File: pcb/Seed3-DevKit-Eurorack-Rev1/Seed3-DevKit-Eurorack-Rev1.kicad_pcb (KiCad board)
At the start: 2 copper layers, 141.9 x 111 mm, 136 parts, among them J7 USB4110GFA, Q1 MMBT3904, Q2 MMBT3904, SW1 TOGGLE_ON_OFF_ON_PIP2, SW2 TOGGLE_ON-ON_PIP3, SW3 PTH Mini Button, SW4 PTH Mini Button, U1 TL072, U11 H11L1, U12 CD4051B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

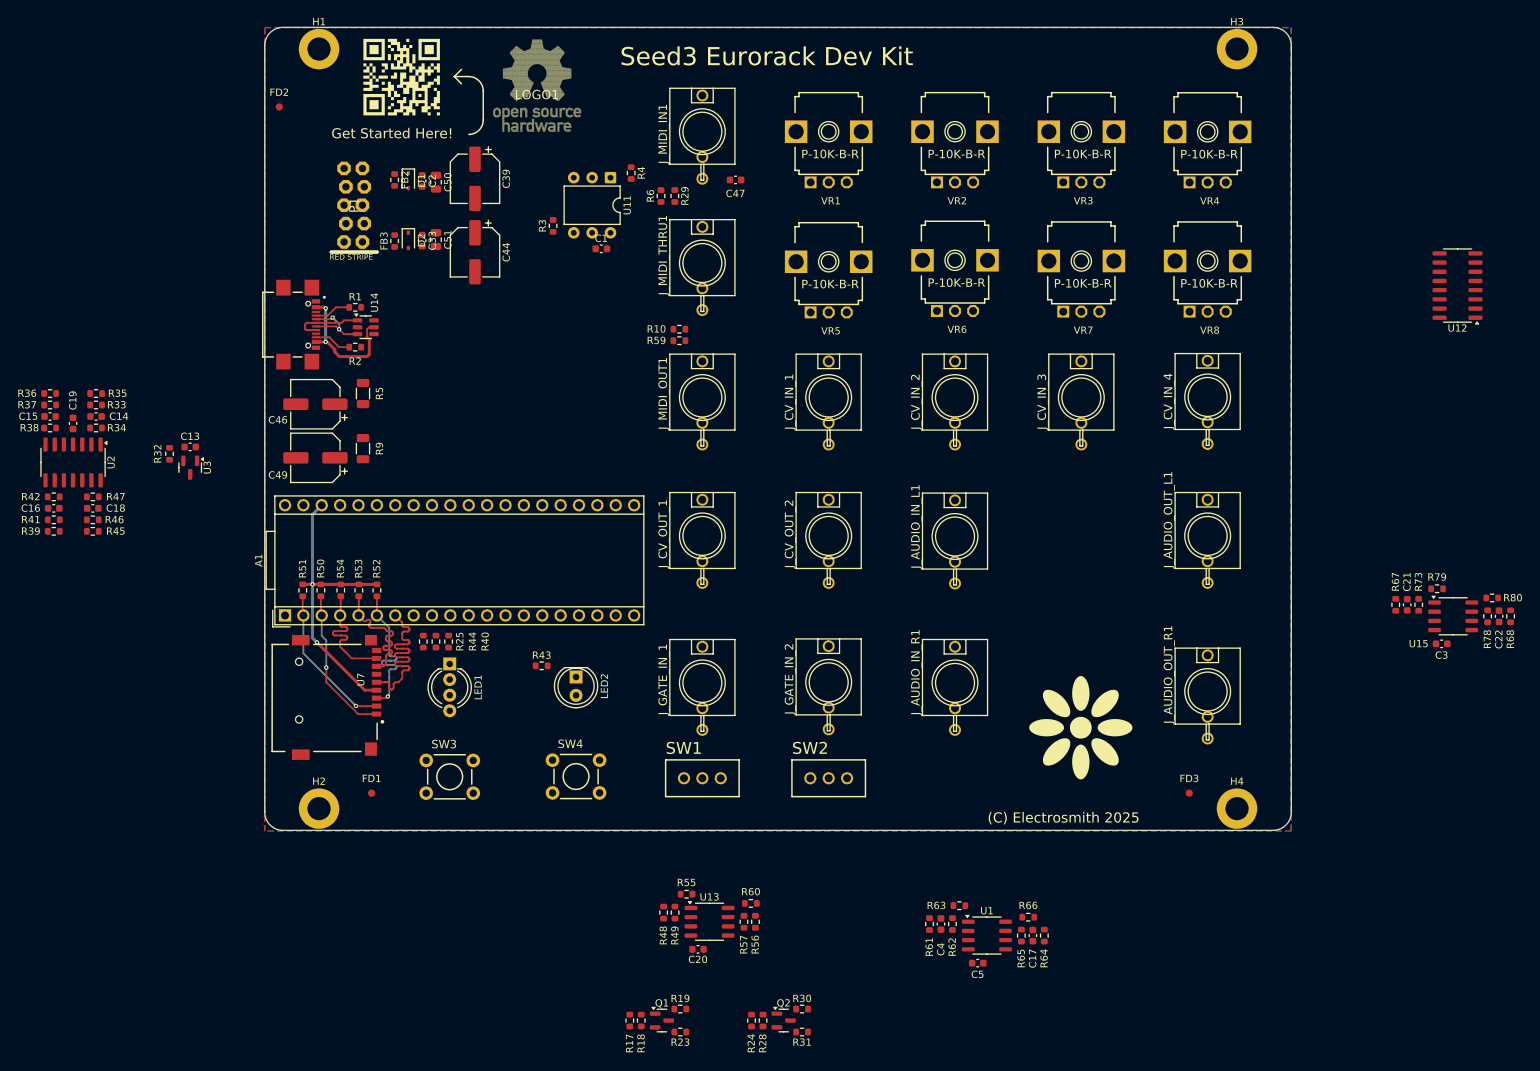
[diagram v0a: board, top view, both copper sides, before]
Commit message: finished routing board, fixed DRCs, and added cutout to PCB.
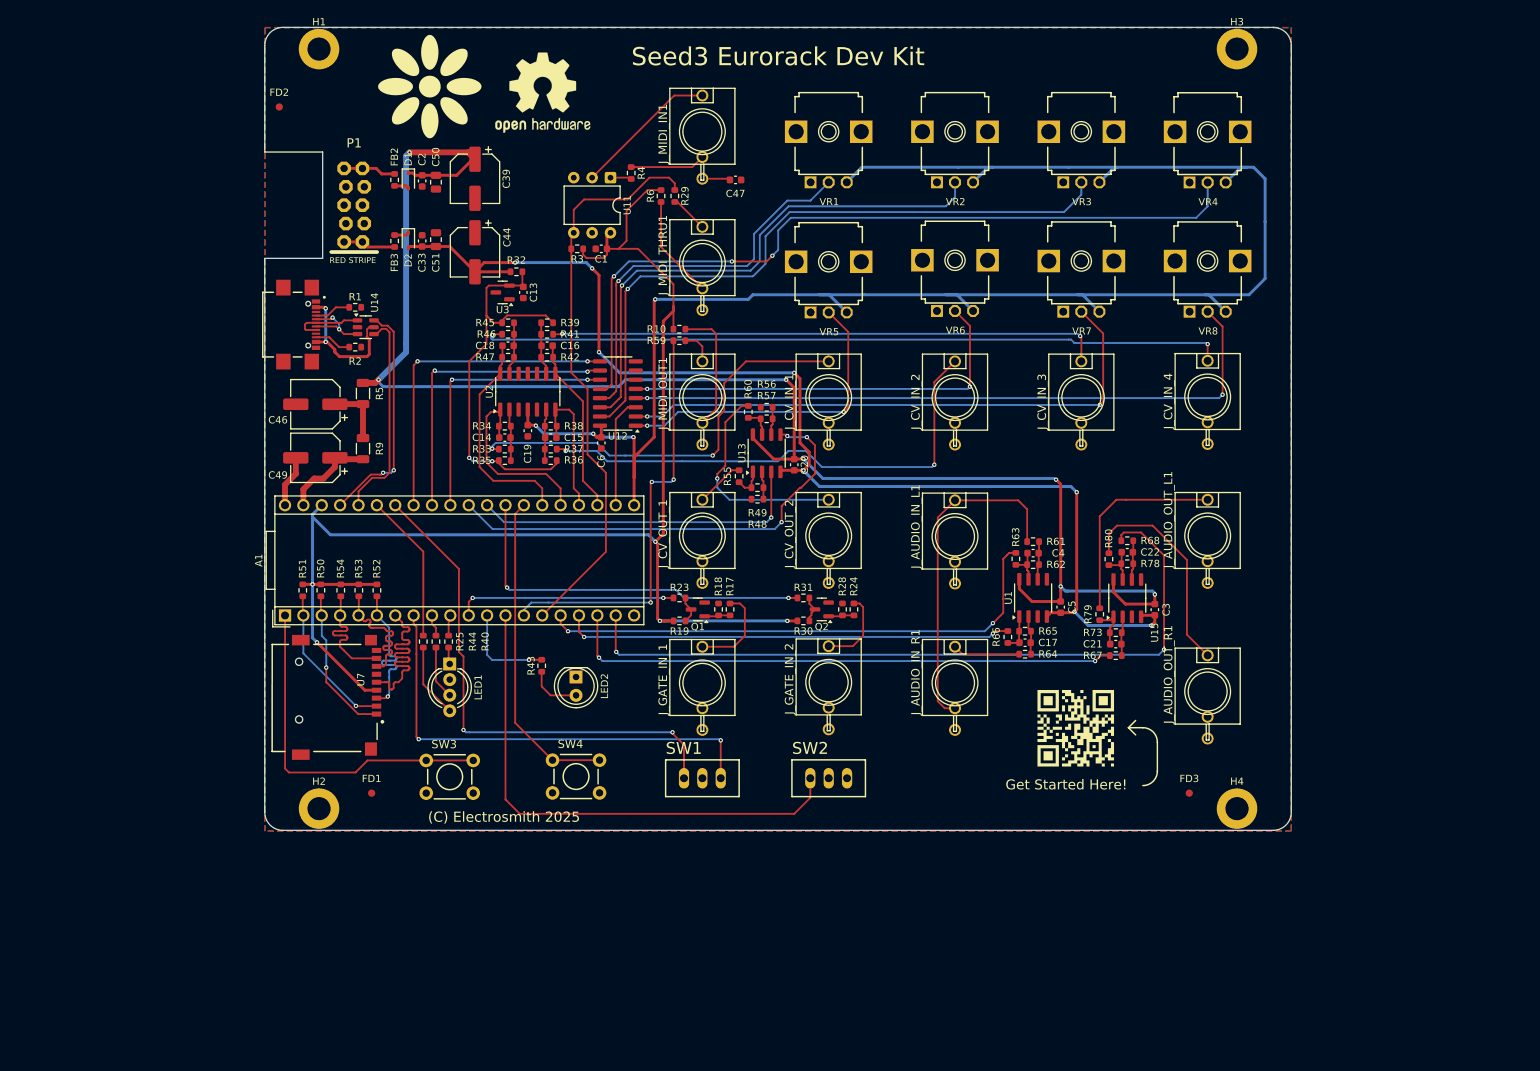
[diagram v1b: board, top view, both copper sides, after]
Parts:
- added C6: 100NF, Capacitor_SMD:C_0603_1608Metric, F.Cu at (96.5, 101.4)
- LOGO1: footprint parts-for-kicad:OSHW-LOGO-L_TEXT -> Symbol:OSHW-Logo2_14.6x12mm_SilkScreen
- SW1: footprint parts-for-kicad:TOGGLE_SILK_PIP3 -> parts-for-kicad:TOGGLE_ON_OFF_ON_SILK
- SW2: footprint parts-for-kicad:TOGGLE_SILK_PIP3 -> parts-for-kicad:TOGGLE_ON-ON_SILK
- VR1, VR2, VR3, VR4, VR5, VR6, VR7, VR8: footprint parts-for-kicad:9MM_SNAP-IN_POT_SILK_PIP -> parts-for-kicad:9MM_SNAP-IN_POT_SILK
- moved U12 117.0 mm to (98.8, 94.6)
- moved R39 74.0 mm to (89.0, 84.8), turned to 0 degrees
- moved R41 72.9 mm to (89.0, 86.4), turned to 0 degrees
- moved C16 71.8 mm to (89.0, 88.0), turned to 180 degrees
- moved R56 71.1 mm to (119.4, 96.5), turned to 180 degrees
- moved R42 70.9 mm to (89.0, 89.6), turned to 180 degrees
- moved R36 69.8 mm to (89.5, 103.9)
- moved R57 69.6 mm to (119.4, 98.1), turned to 0 degrees
- moved R37 69.5 mm to (89.5, 102.3), turned to 0 degrees
- moved C15 69.3 mm to (89.5, 100.7), turned to 180 degrees
- moved R38 69.2 mm to (89.5, 99.1), turned to 180 degrees
- moved C20 68.3 mm to (123.2, 104.5), turned to -90 degrees
- moved R60 67.9 mm to (116.8, 97.2), turned to -90 degrees
- moved U13 65.3 mm to (119.4, 102.9), turned to 90 degrees
- moved R45 64.2 mm to (83.6, 84.8), turned to 180 degrees
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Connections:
- A1 pad 10: TOG_1 -> LED_R
- A1 pad 13: /Daisy/MUX_CTRL_C -> TOG_1
- A1 pad 23: /Daisy/CV_1_ADC -> /Daisy/CV_3_ADC
- A1 pad 25: /Daisy/CV_3_ADC -> /Daisy/CV_1_ADC
- A1 pad 33: LED_R -> /Daisy/MUX_CTRL_C
- A1 pad 34: LED_B -> TOG_2_A
- A1 pad 9: TOG_2_A -> LED_B
- C17 pad 2: Net-(U1B--) -> Net-(U1A--)
- C4 pad 2: Net-(U1A--) -> Net-(U1B--)
- H1 pad 1: (no net) -> unconnected-(H1-Pad1)
- H2 pad 1: (no net) -> unconnected-(H2-Pad1)
- H3 pad 1: (no net) -> unconnected-(H3-Pad1)
- H4 pad 1: (no net) -> unconnected-(H4-Pad1)
- R61 pad 1: Net-(U1A--) -> Net-(U1B--)
- R62 pad 2: Net-(U1A--) -> Net-(U1B--)
- R64 pad 1: Net-(U1B--) -> Net-(U1A--)
- R65 pad 2: Net-(U1B--) -> Net-(U1A--)
- U1 pad 1: Net-(C4-Pad1) -> Net-(C17-Pad1)
- U1 pad 7: Net-(C17-Pad1) -> Net-(C4-Pad1)
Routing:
- net +3V3_A: track 0.00 -> 242.2 mm, vias 0 -> 4
- net +12V: track 0.00 -> 217.2 mm, vias 0 -> 7
- net -12V: track 0.00 -> 165.6 mm, vias 0 -> 8
- net +3V3: track 41.0 -> 192.6 mm, vias 2 -> 5
- net POT_4: track 0.00 -> 107.9 mm, vias 0 -> 3
- net Net-(J_CV_IN_4-PadTIP): track 0.00 -> 103.6 mm, vias 0 -> 2
- net /Daisy/CODEC_OUT_R: track 0.00 -> 102.4 mm, vias 0 -> 2
- net POT_8: track 0.00 -> 93.6 mm, vias 0 -> 2
- net POT_3: track 0.00 -> 92.0 mm, vias 0 -> 1
- net POT_7: track 0.00 -> 79.1 mm, vias 0 -> 2
- net MIDI_RX: track 0.00 -> 79.1 mm
- net /Daisy/CODEC_OUT_L: track 0.00 -> 77.1 mm, vias 0 -> 2
- net Net-(J_CV_IN_3-PadTIP): track 0.00 -> 76.6 mm, vias 0 -> 2
- net POT_2: track 0.00 -> 74.2 mm, vias 0 -> 1
- net /Daisy/CODEC_IN_L: track 0.00 -> 73.4 mm, vias 0 -> 2
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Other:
- outline, holes or cut-outs redrawn

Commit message: added missing board info, and regenerated prod mats.
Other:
- board text added: "0"
- board text added: "0 mm"
- board text added: "0.0000 mm / 0.1524 mm"
- board text added: "0.01 mm"
- board text added: "0.02"
- board text added: "0.035 mm"
- board text added: "0.3000 mm"
- board text added: "1"
- board text added: "1.51 mm"
- board text added: "1.6000 mm"
- board text added: "141.9000 mm x 111.0000 mm"
- board text added: "2"
- board text added: "4.5"
- board text added: "B.Cu"
- board text added: "B.Mask"
- board text added: "B.Paste"
- board text added: "B.Silkscreen"
- board text added: "BOARD CHARACTERISTICS"
- board text added: "Black"
- board text added: "Board Thickness:"
- board text added: "Board overall dimensions:"
- board text added: "Bottom Silk Screen"
- board text added: "Bottom Solder Mask"
- board text added: "Bottom Solder Paste"
- board text added: "Castellated pads:"
- board text added: "Color"
- board text added: "Copper Finish:"
- board text added: "Copper Layer Count:"
- board text added: "Dielectric"
- board text added: "ENIG"
- board text added: "Edge card connectors:"
- board text added: "Epsilon R"
- board text added: "F.Cu"
- board text added: "F.Mask"
- board text added: "F.Paste"
- board text added: "F.Silkscreen"
- board text added: "FR4"
- board text added: "Impedance Control:"
- board text added: "Layer Name"
- board text added: "Loss Tangent"
- board text added: "Material"
- board text added: "Matte"
- board text added: "Min hole diameter:"
- board text added: "Min track/spacing:"
- board text added: "No"
- board text added: "Not specified"
- board text added: "Plated Board Edge:"
- board text added: "Thickness (mm)"
- board text added: "Top Silk Screen"
- board text added: "Top Solder Mask"
- board text added: "Top Solder Paste"
- board text added: "Type"
- board text added: "White"
- board text added: "copper"
- board text added: "core"

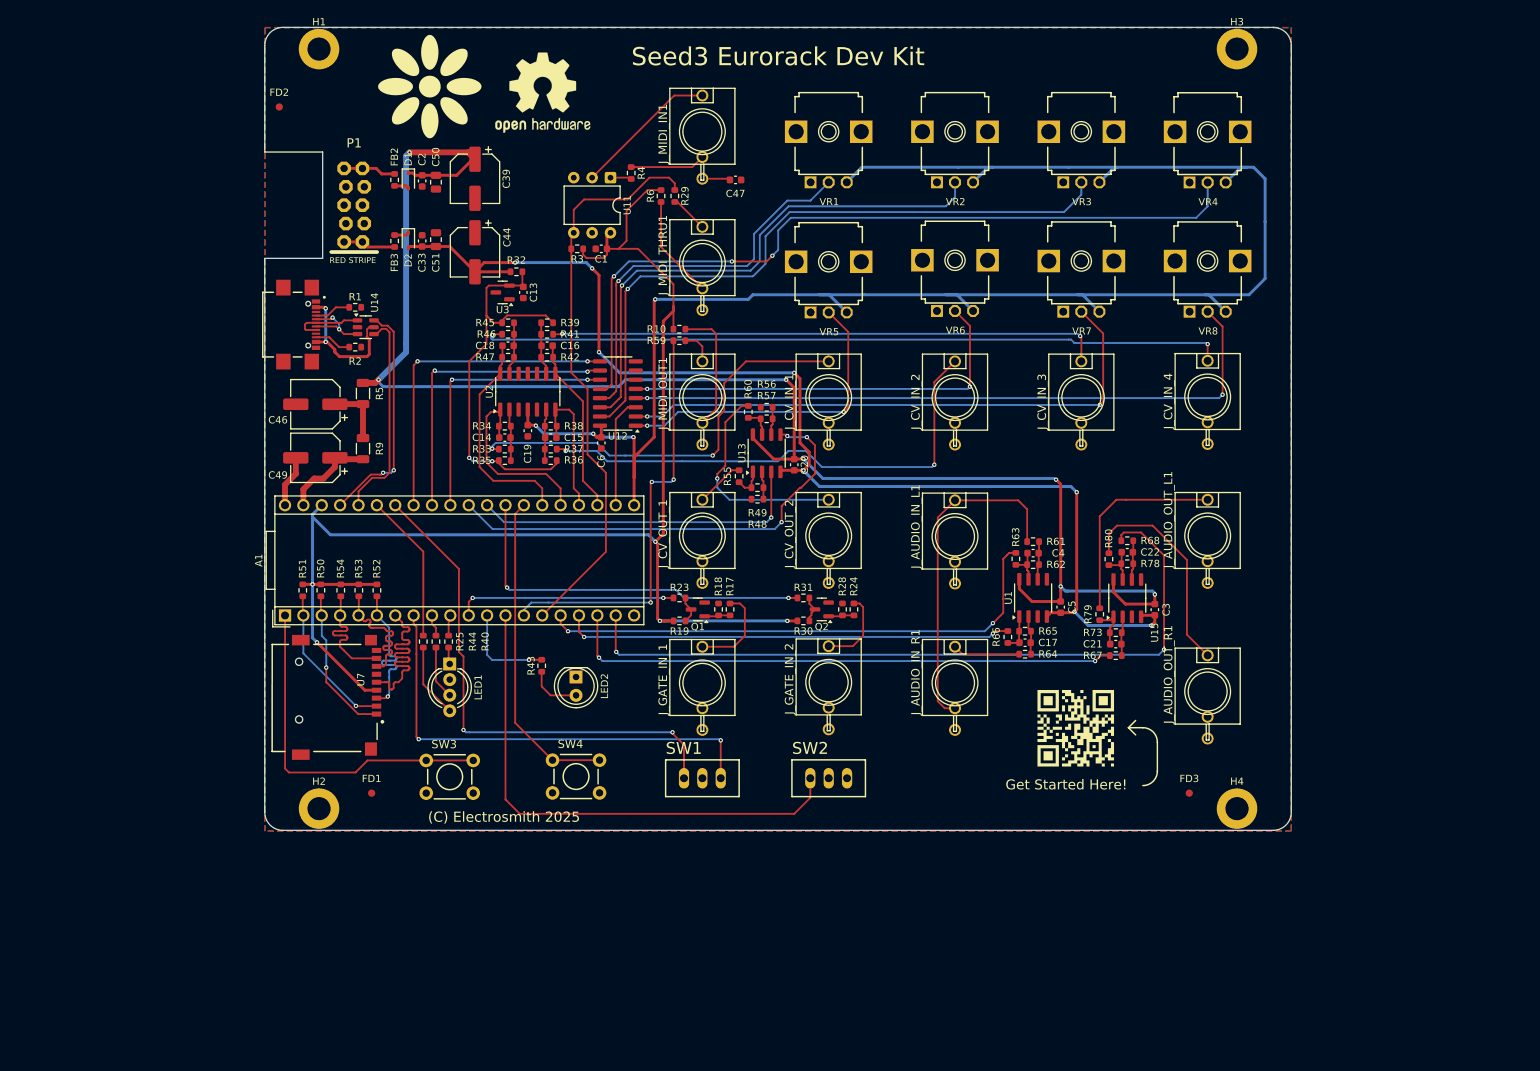
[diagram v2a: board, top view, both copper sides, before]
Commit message: a lot of little silk changes.
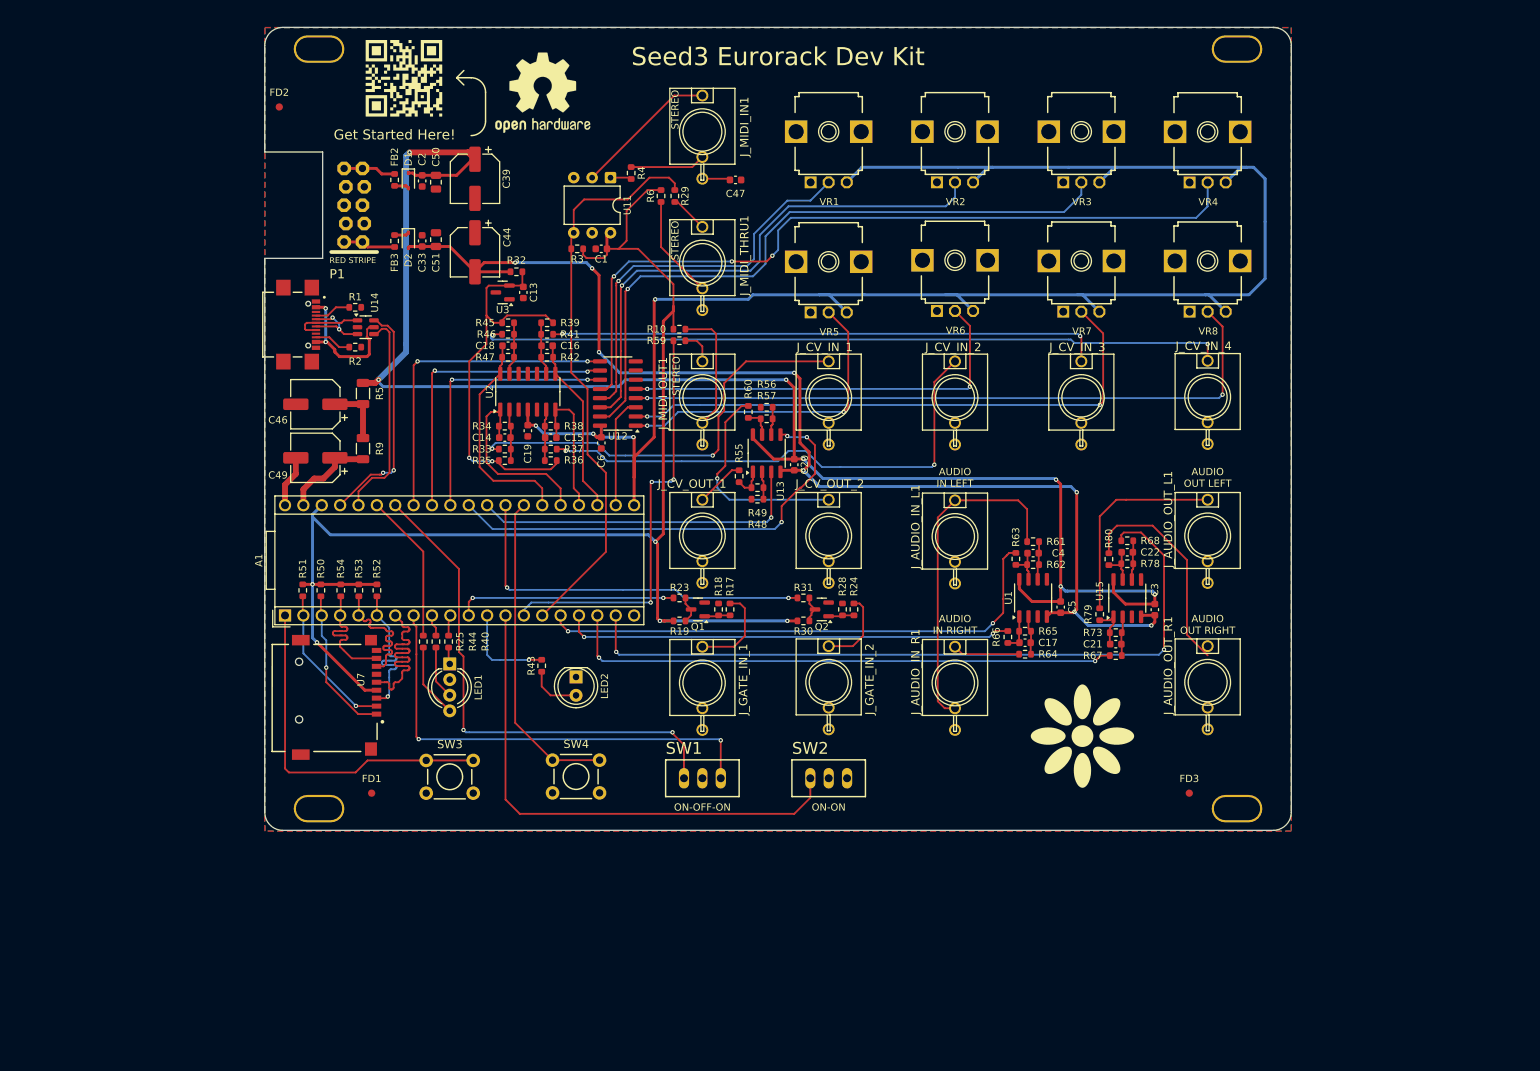
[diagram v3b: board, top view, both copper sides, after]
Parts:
- H1, H2, H3, H4: footprint MountingHole:MountingHole_3.2mm_M3_DIN965_Pad -> shnsly:MNT_SLOT_M3_PLATED
- moved J_AUDIO_OUT_R1 1.27 mm to (180.3, 134.5)
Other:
- board text added: "(C) Daisy 2025"
- board text added: "AUDIO IN LEFT"
- board text added: "AUDIO IN RIGHT"
- board text added: "AUDIO OUT LEFT"
- board text added: "AUDIO OUT RIGHT"
- board text added: "ON-OFF-ON"
- board text added: "ON-ON"
- board text added: "STEREO"
- board text removed: "(C) Electrosmith 2025"
